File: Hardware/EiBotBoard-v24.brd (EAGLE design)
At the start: 56.9 x 56.9 mm, 99 parts, among them IC1 A4988ALT1, IC2 A4988ALT1, IC3 PIC18F46J50-I/PT, IC4 V_REG_317DPACK, IC5 V_REG_317DPACK

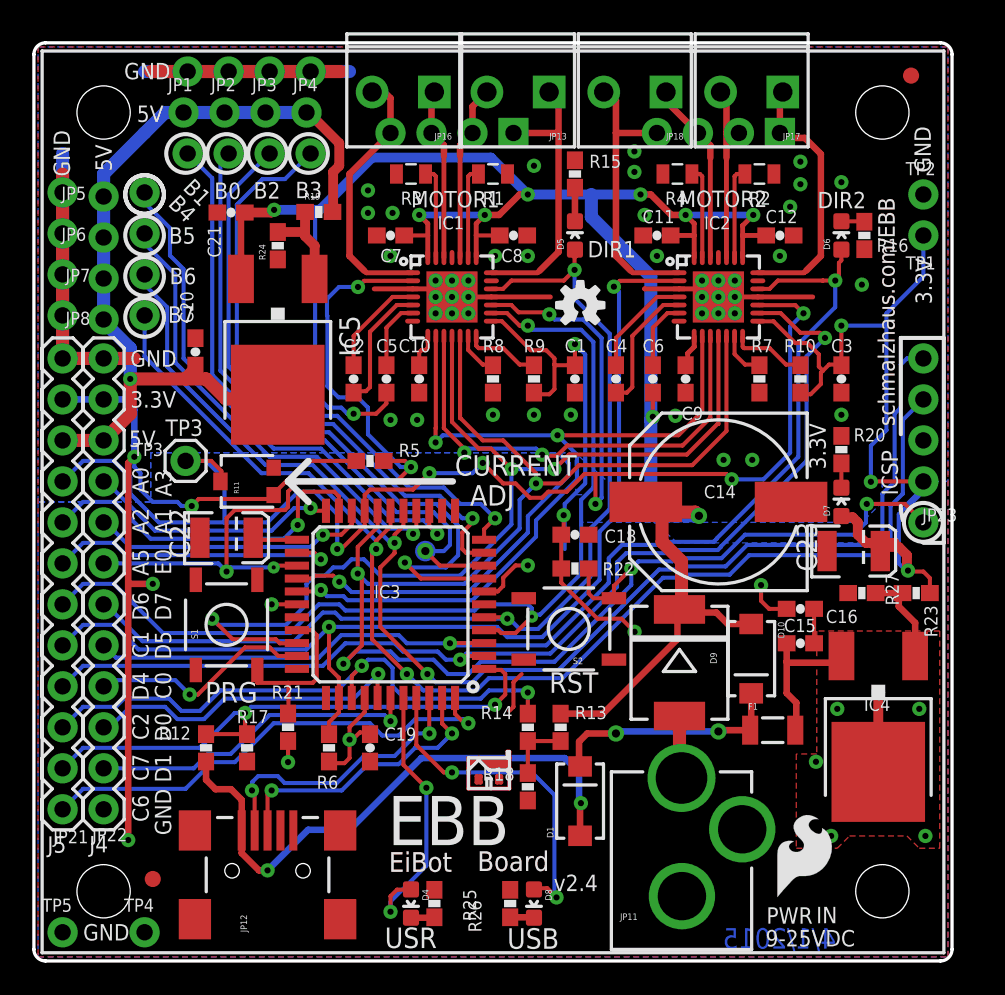
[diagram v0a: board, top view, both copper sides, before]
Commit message: Updated board and schematic as per Peter Lewis' design review nodes (issue #1 in GitHub)
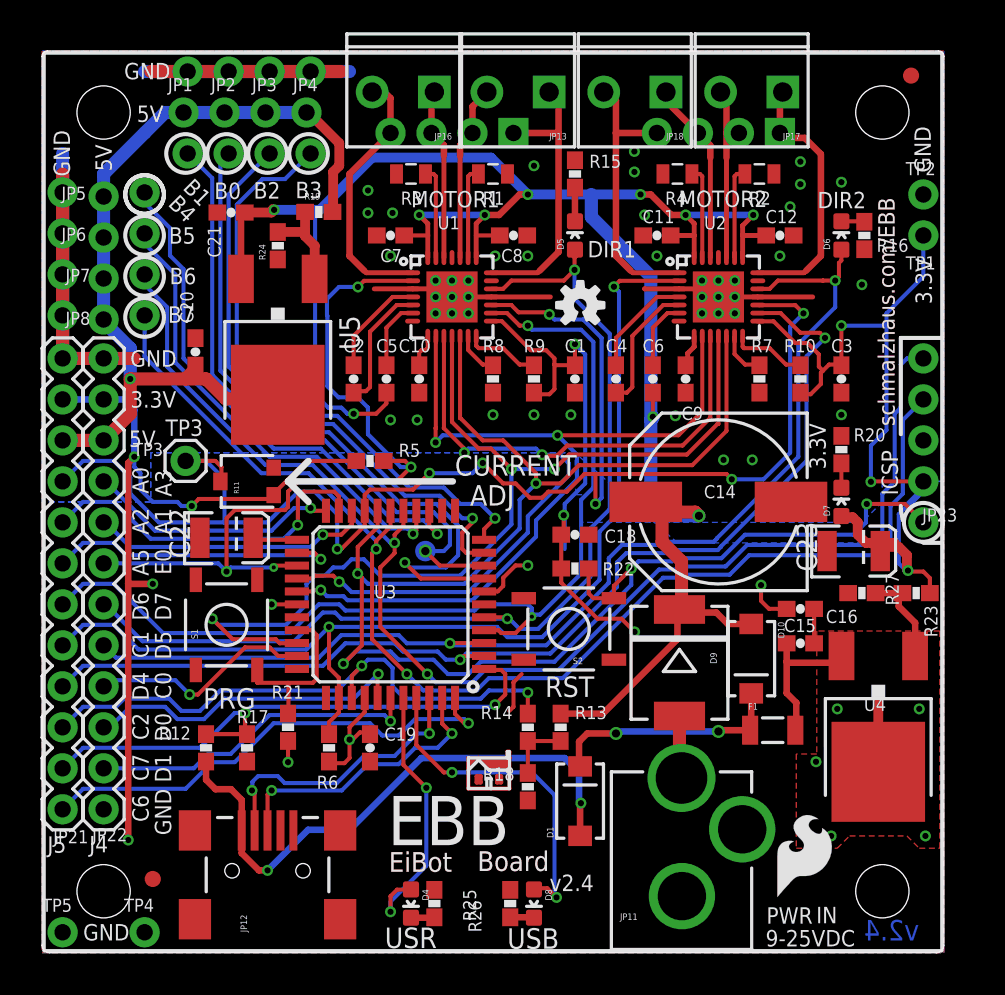
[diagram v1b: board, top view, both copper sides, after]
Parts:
- moved LOGO3 9.26 mm to (54.9, 15.5)
- renumbered IC1 to U1, IC2 to U2, IC3 to U3, IC4 to U4, IC5 to U5
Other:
- board size 56.9 x 56.9 mm -> 55.9 x 55.9 mm
- board text removed: "4/1/2015"

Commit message: Reverted LEDs back to their original colors, removed outline line on tPlace, made outline on dimension layer 0.008" wide, switched driver chip footprints to A4988ALT1_REDUCED_PASTE.
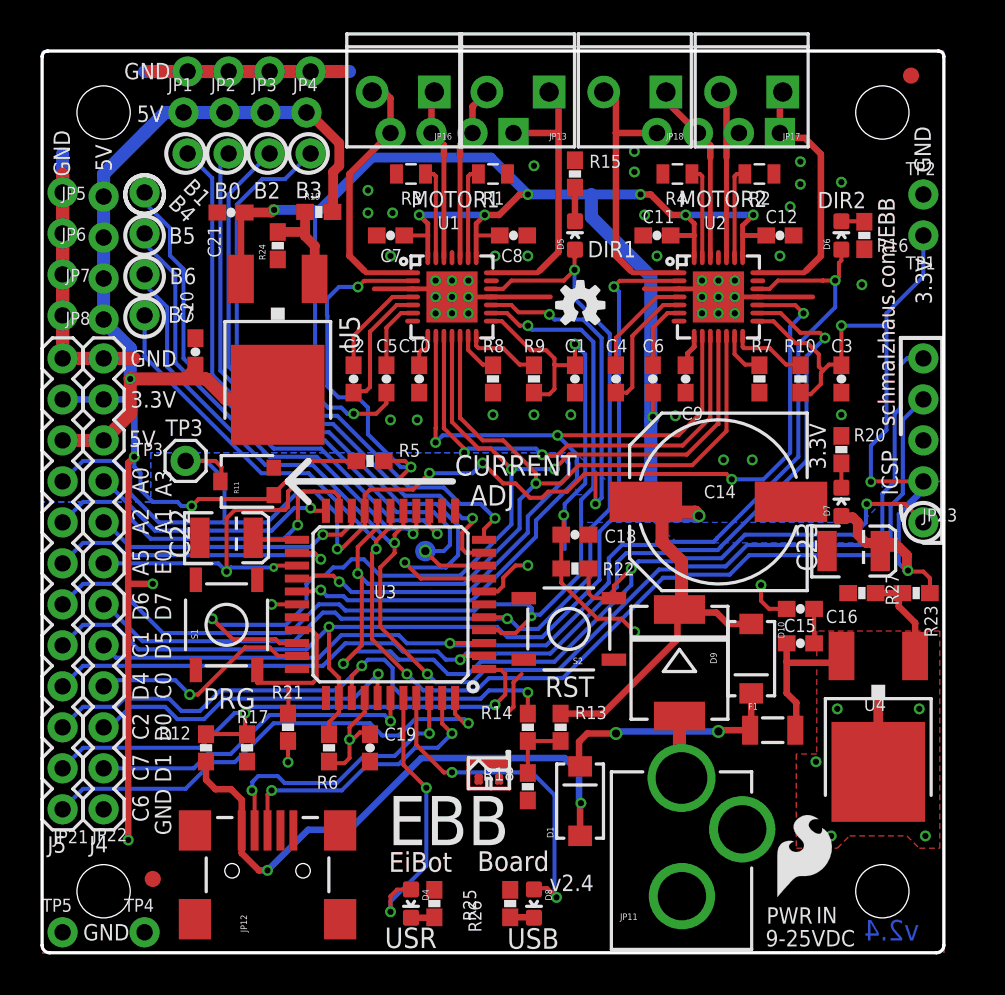
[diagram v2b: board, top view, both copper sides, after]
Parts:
- D5, D6: value GREEN -> RED
- D7, D8: value RED -> GREEN
- U1, U2: value A4988ALT1 -> A4988ALT1_REDUCED_PASTE; device SparkFun-PowerIC:QFN-28-5MM_ALT1 -> SparkFun-PowerIC:QFN-28-5MM_ALT1_REDUCED_PASTE

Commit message: Added MAX direction indication on top silk for current adjust pot.
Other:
- board text added: "MAX"
